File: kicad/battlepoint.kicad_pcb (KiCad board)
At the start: 2 copper layers, 101.6 x 153.7 mm, 28 parts, among them J1 BTNS, J2 TMR_LEDS, J3 CAP_LEDS, P13 BTNS_IN, P14 OLED_OUT, P17 BTNS_OUT, P20 AUX_PWR, P30 EXT_PWR_JP, P31 CONN_01X12, P35 CONN_01X12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

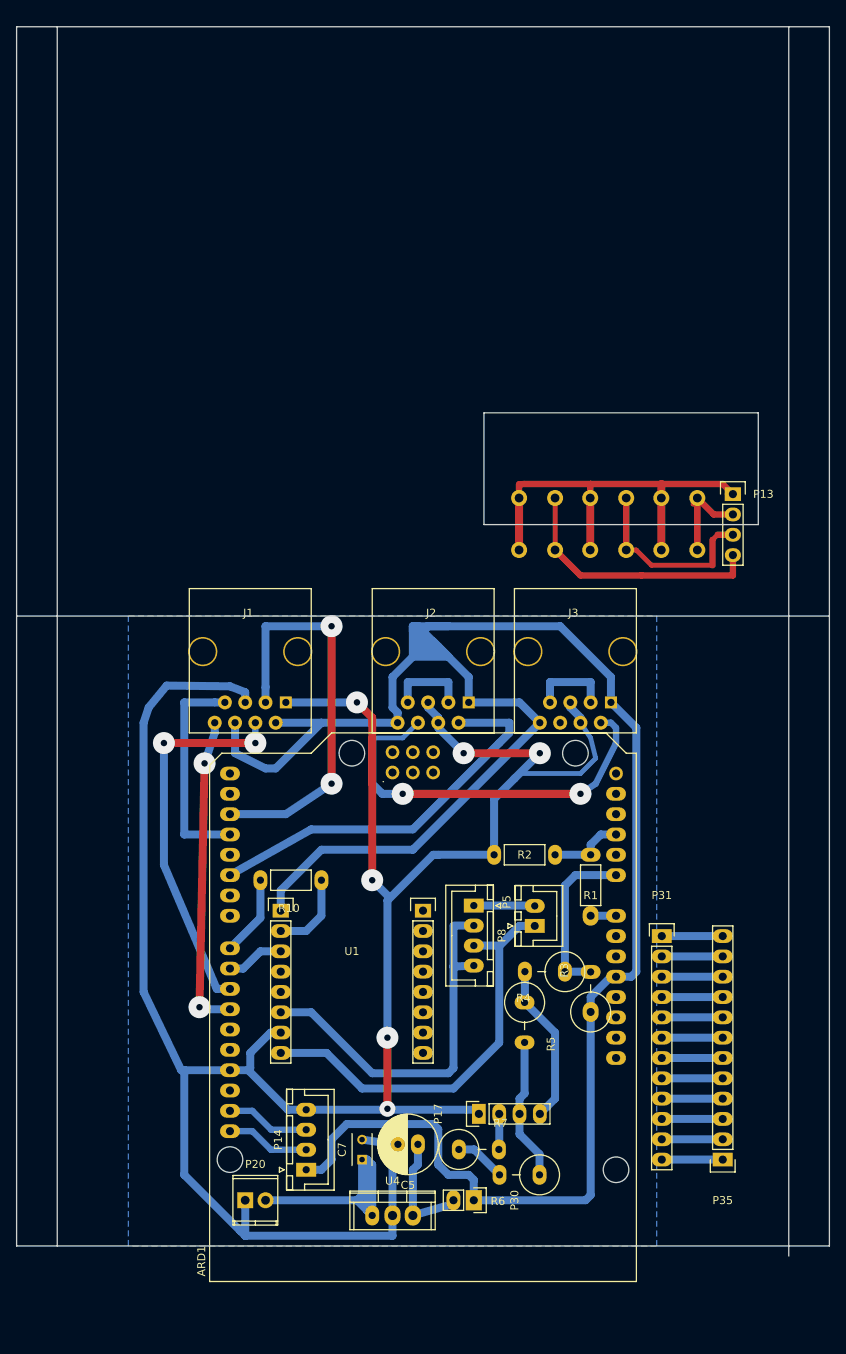
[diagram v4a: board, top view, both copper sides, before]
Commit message: changed to usb connectors
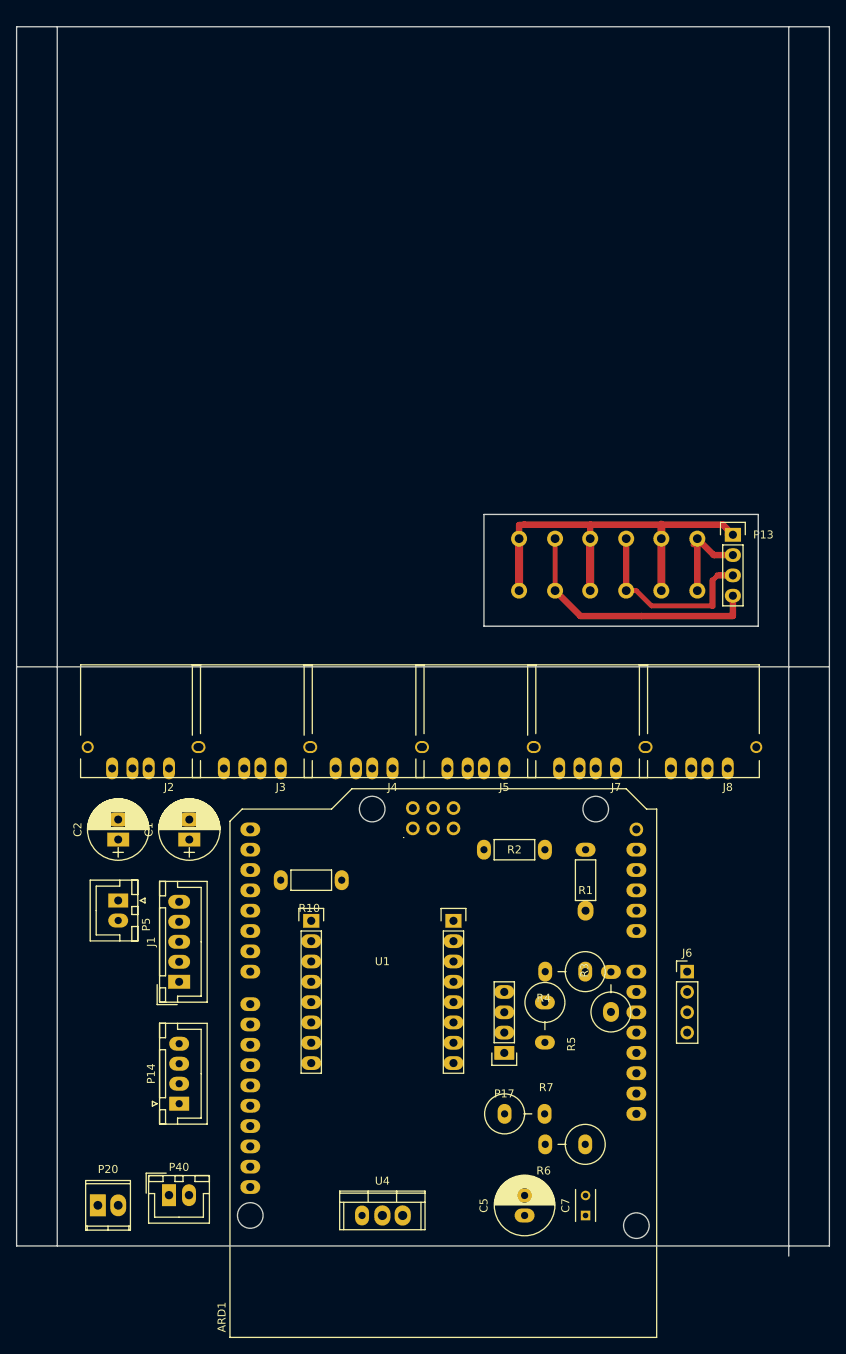
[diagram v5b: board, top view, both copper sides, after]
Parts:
- removed P30: EXT_PWR_JP, Pin_Headers:Pin_Header_Straight_1x02
- removed P31, P35: CONN_01X12, Pin_Headers:Pin_Header_Straight_1x12
- removed P8: AUDIO_JACK, Connectors_JST:JST_XH_B04B-XH-A_04x2.50mm_Straight
- added C1: 1000uf, Capacitors_THT:CP_Radial_D7.5mm_P2.50mm, F.Cu at (40.6, 143.5)
- added C2: 1000uf, Capacitors_THT:CP_Radial_D7.5mm_P2.50mm, F.Cu at (31.8, 143.5)
- added J4: TMR1_LED, Connectors:USB_A, F.Cu at (66.0, 134.6)
- added J5: TMR2_LED, Connectors:USB_A, F.Cu at (80.0, 134.6)
- added J6: PWR_OPTION, Pin_Headers:Pin_Header_Straight_1x04_Pitch2.54mm, F.Cu at (102.9, 160.0)
- added J7: CAP_LED, Connectors:USB_A, F.Cu at (94.0, 134.6)
- added J8: OWN_LED, Connectors:USB_A, F.Cu at (108.0, 134.6)
- added P40: PWR_SWITCH, Connectors_JST:JST_XH_B02B-XH-A_02x2.50mm_Straight, F.Cu at (38.1, 188.0)
- J1: value BTNS -> AUDIO; footprint Connect:RJ45_8 -> Connectors_JST:JST_XH_B05B-XH-A_05x2.50mm_Straight
- J2: value TMR_LEDS -> BLU_SWITCH; footprint Connect:RJ45_8 -> Connectors:USB_A
- J3: value CAP_LEDS -> RED_SWITCH; footprint Connect:RJ45_8 -> Connectors:USB_A
- P20: value AUX_PWR -> BATT
- moved P5 52.2 mm to (31.8, 151.1), turned to 270 degrees
- moved J1 42.2 mm to (39.4, 161.3), turned to 90 degrees
- moved J3 39.6 mm to (52.1, 134.6)
- moved J2 36.1 mm to (38.1, 134.6)
- moved C7 28.8 mm to (90.2, 190.5)
- moved P20 18.4 mm to (29.2, 189.2)
- moved P14 17.9 mm to (39.4, 176.5)
- moved C5 16.0 mm to (82.5, 190.5), turned to 90 degrees
- moved P17 8.26 mm to (80.0, 170.2), turned to 180 degrees
- moved ARD1 7.43 mm to (99.1, 205.7)
- moved R7 7.24 mm to (82.5, 177.8)
- moved R6 6.87 mm to (87.6, 181.6)
- moved P13 5.08 mm to (108.6, 105.4)
- moved SW1 5.08 mm to (86.4, 112.4)
- moved SW2 5.08 mm to (95.2, 112.4)
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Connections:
- ARD1 pad VIN: Net-(ARD1-PadVIN) -> VIN
- C5 pad 1: Net-(C5-Pad1) -> +5VA
- J1 pad 2: +5V -> Net-(J1-Pad2)
- J1 pad 3: D2 -> Net-(J1-Pad3)
- J1 pad 4: D10 -> Net-(J1-Pad4)
- J1 pad 5: GND -> Net-(J1-Pad5)
- J2 pad 1: +5V -> +5VA
- J2 pad 2: D5 -> D10
- J2 pad 3: Net-(J2-Pad3) -> D2
- J2 pad 5: GND -> Net-(J2-Pad5)
- J3 pad 1: +5V -> +5VA
- J3 pad 2: Net-(J2-Pad6) -> D11
- J3 pad 3: Net-(J3-Pad3) -> D3
- J3 pad 5: GND -> Net-(J3-Pad5)
- P20 pad 2: Net-(C7-Pad1) -> Net-(P20-Pad2)
- P5 pad 1: Net-(P5-Pad1) -> Net-(J1-Pad5)
- P5 pad 2: Net-(P5-Pad2) -> Net-(J1-Pad4)
- R1 pad 1: Net-(ARD1-PadVIN) -> VBATT
- U1 pad 6: Net-(P8-Pad2) -> Net-(J1-Pad3)
- U1 pad 8: Net-(P5-Pad1) -> Net-(J1-Pad2)
- U4 pad 3: Net-(C5-Pad1) -> +5VA
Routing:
- net GND: track 356.6 -> 55.1 mm, vias 6 -> 0
- net +5V: track 282.2 -> 0.00 mm
- net Net-(P5-Pad1): track 52.3 -> 0.00 mm
- net D2: track 51.3 -> 0.00 mm, vias 2 -> 0
- net Net-(J2-Pad6): track 50.8 -> 0.00 mm, vias 2 -> 0
- net D5: track 49.0 -> 0.00 mm
- net Net-(P8-Pad2): track 47.9 -> 0.00 mm
- net D10: track 47.7 -> 0.00 mm, vias 2 -> 0
- net D11: track 39.7 -> 0.00 mm, vias 2 -> 0
- net Net-(C7-Pad1): track 35.9 -> 0.00 mm
- net D3: track 27.3 -> 0.00 mm
- net A0: track 20.9 -> 0.00 mm
- net Net-(P17-Pad4): track 20.2 -> 0.00 mm
- net Net-(P17-Pad3): track 17.8 -> 0.00 mm
- net Net-(C5-Pad1): track 14.7 -> 0.00 mm
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- removed copper zone on B.Cu, net GND
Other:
- outline, holes or cut-outs redrawn

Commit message: routed
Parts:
- J2: value BLU_SWITCH -> RED_SWITCH; footprint Connectors:USB_A -> Connectors_JST:JST_XH_B04B-XH-A_04x2.50mm_Straight
- J3: value RED_SWITCH -> BLU_SWITCH; footprint Connectors:USB_A -> Connectors_JST:JST_XH_B04B-XH-A_04x2.50mm_Straight
- J4: value TMR1_LED -> LED1; footprint Connectors:USB_A -> Connectors_JST:JST_XH_B04B-XH-A_04x2.50mm_Straight
- J5: value TMR2_LED -> LED2; footprint Connectors:USB_A -> Connectors_JST:JST_XH_B04B-XH-A_04x2.50mm_Straight
- J7: value CAP_LED -> LED3; footprint Connectors:USB_A -> Connectors_JST:JST_XH_B04B-XH-A_04x2.50mm_Straight
- J8: value OWN_LED -> LED4; footprint Connectors:USB_A -> Connectors_JST:JST_XH_B04B-XH-A_04x2.50mm_Straight
- P17: footprint Pin_Headers:Pin_Header_Straight_1x04 -> Connectors_JST:JST_XH_B04B-XH-A_04x2.50mm_Straight
- P20: footprint Terminal_Blocks:TerminalBlock_Pheonix_MPT-2.54mm_2pol -> Connectors_JST:JST_XH_B02B-XH-A_02x2.50mm_Straight
- moved C7 55.7 mm to (34.9, 183.5), turned to 180 degrees
- moved J1 40.1 mm to (78.7, 153.7), turned to 180 degrees
- moved P5 38.4 mm to (69.8, 146.1), turned to 0 degrees
- moved C1 18.9 mm to (36.2, 125.1), turned to 270 degrees
- moved C2 18.7 mm to (28.6, 125.1), turned to 270 degrees
- moved J8 11.6 mm to (96.5, 132.7), turned to 90 degrees
- moved R10 9.16 mm to (64.8, 156.2)
- moved R5 8.98 mm to (91.4, 172.7)
- moved J7 7.85 mm to (86.4, 132.7), turned to 90 degrees
- moved U1 7.43 mm to (57.1, 160.7)
- moved P14 7.24 mm to (33.7, 172.1), turned to 0 degrees
- moved C5 6.25 mm to (76.8, 188.0)
- moved J2 5.43 mm to (43.2, 132.7), turned to 90 degrees
- moved R2 5.24 mm to (86.4, 139.7)
- moved J5 4.26 mm to (76.2, 132.7), turned to 90 degrees
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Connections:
- C1 pad 1: Net-(C1-Pad1) -> +5VA
- C2 pad 1: Net-(C1-Pad1) -> +5VA
- C7 pad 1: Net-(C7-Pad1) -> VBATT
- J2 pad 1: +5VA -> GND
- J2 pad 4: GND -> +5VA
- J3 pad 1: +5VA -> GND
- J3 pad 4: GND -> +5VA
- J4 pad 1: +5VA -> GND
- J4 pad 2: Net-(J4-Pad2) -> D5
- J4 pad 3: D5 -> Net-(J4-Pad3)
- J4 pad 4: GND -> +5VA
- J5 pad 1: +5VA -> GND
- J5 pad 2: Net-(J5-Pad2) -> Net-(J4-Pad3)
- J5 pad 3: Net-(J4-Pad2) -> Net-(J5-Pad3)
- J5 pad 4: GND -> +5VA
- J6 pad 1: Net-(C7-Pad1) -> VBATT
- J7 pad 1: +5VA -> GND
- J7 pad 2: Net-(J7-Pad2) -> Net-(J5-Pad3)
- J7 pad 3: Net-(J5-Pad2) -> Net-(J7-Pad3)
- J7 pad 4: GND -> +5VA
- J8 pad 1: +5VA -> GND
- J8 pad 2: Net-(J8-Pad2) -> Net-(J7-Pad3)
- J8 pad 3: Net-(J7-Pad2) -> Net-(J8-Pad3)
- J8 pad 4: GND -> +5VA
- P40 pad 2: Net-(C7-Pad1) -> VBATT
- U4 pad 1: Net-(C7-Pad1) -> VBATT
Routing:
- net GND: track 55.1 -> 385.1 mm
- net +5VA: track 0.00 -> 193.4 mm
- net VBATT: track 0.00 -> 158.1 mm, vias 0 -> 2
- net +5V: track 0.00 -> 143.1 mm, vias 0 -> 2
- net D11: track 0.00 -> 49.5 mm, vias 0 -> 2
- net D10: track 0.00 -> 46.0 mm, vias 0 -> 2
- net D5: track 0.00 -> 37.7 mm, vias 0 -> 2
- net Net-(J1-Pad2): track 0.00 -> 35.2 mm
- net Net-(J1-Pad3): track 0.00 -> 29.0 mm
- net D3: track 0.00 -> 28.9 mm
- net D2: track 0.00 -> 27.0 mm
- net SCL: track 0.00 -> 21.2 mm
- net Net-(P17-Pad3): track 0.00 -> 20.6 mm
- net Net-(P17-Pad4): track 0.00 -> 17.9 mm
- net D8: track 0.00 -> 17.6 mm, vias 0 -> 2
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- added copper zone on B.Cu, net +5VA
- added copper zone on B.Cu, net GND
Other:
- board size 101.6 x 153.7 mm -> 101.6 x 154.3 mm
- net class BIG: trace_width 1 -> 0.8
- net class Default: trace_width 1 -> 0.8
- net class SMALL: trace_width 0.3 -> 0.5
- rule trace_min: 0.2 -> 0.5
- rule via_min_size: 0.4 -> 0.5

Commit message: finished routing
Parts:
- added P1: A_LED1, Connectors_JST:JST_XH_B04B-XH-A_04x2.50mm_Straight, F.Cu at (30.5, 113.7)
- added P2: A_LED2, Connectors_JST:JST_XH_B04B-XH-A_04x2.50mm_Straight, F.Cu at (40.6, 113.7)
- added P3: A_LED3, Connectors_JST:JST_XH_B04B-XH-A_04x2.50mm_Straight, F.Cu at (49.5, 113.7)
- added P4: A_LED_4, Connectors_JST:JST_XH_B04B-XH-A_04x2.50mm_Straight, F.Cu at (59.1, 113.7)
- added P6: A_LED5, Connectors_JST:JST_XH_B04B-XH-A_04x2.50mm_Straight, F.Cu at (68.6, 113.7)
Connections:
- J4 pad 1: GND -> Net-(J4-Pad1)
- J4 pad 3: Net-(J4-Pad3) -> GND
- J5 pad 1: GND -> Net-(J5-Pad1)
- J5 pad 2: Net-(J4-Pad3) -> Net-(J4-Pad1)
- J5 pad 3: Net-(J5-Pad3) -> GND
- J7 pad 1: GND -> Net-(J7-Pad1)
- J7 pad 2: Net-(J5-Pad3) -> Net-(J5-Pad1)
- J7 pad 3: Net-(J7-Pad3) -> GND
- J8 pad 1: GND -> Net-(J8-Pad1)
- J8 pad 2: Net-(J7-Pad3) -> Net-(J7-Pad1)
- J8 pad 3: Net-(J8-Pad3) -> GND
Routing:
- net GND: track 385.1 -> 453.0 mm, vias 0 -> 2
- net +5VA: track 193.4 -> 231.5 mm
- net Net-(J7-Pad3): track 11.5 -> 0.00 mm
- net Net-(P1-Pad1): track 0.00 -> 11.2 mm
- net Net-(J5-Pad3): track 11.2 -> 0.00 mm
- net Net-(J7-Pad1): track 0.00 -> 11.2 mm
- net Net-(J5-Pad1): track 0.00 -> 11.2 mm
- net Net-(J4-Pad3): track 11.2 -> 0.00 mm
- net Net-(J4-Pad1): track 0.00 -> 11.2 mm
- net Net-(P4-Pad1): track 0.00 -> 10.6 mm
- net Net-(P3-Pad1): track 0.00 -> 10.6 mm
- net Net-(P2-Pad1): track 0.00 -> 9.93 mm
- net D2: track 27.0 -> 28.2 mm
- net D11: track 49.5 -> 50.4 mm
- net D10: track 46.0 -> 46.8 mm
